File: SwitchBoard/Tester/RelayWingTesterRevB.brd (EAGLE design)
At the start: 77.1 x 67.3 mm, 18 parts

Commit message: Updating tester
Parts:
- added 3VPIN, GNDPIN, SCLPIN, SDAPIN: (no value), adafruit:1X01
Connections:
- removed net N$18: JP2.1, MS1.1
- new net RESET: JP2.1, MS1.1, U$4.14/A0
- net 3V: now also 3VPIN.1
- net GND: now also GNDPIN.1
- net N$2: now also SDAPIN.1
- net SCL: now also SCLPIN.1
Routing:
- net RESET: track 0.00 -> 74.7 mm, vias 0 -> 1
- net 3V: track 101.5 -> 141.5 mm, vias 0 -> 1
- net GND: track 59.1 -> 91.9 mm
- net SCL: track 40.5 -> 54.0 mm
- net N$2: track 46.6 -> 52.8 mm
- net N$56: track 43.1 -> 45.9 mm
- net N$18: track 2.54 -> 0.00 mm
- net N$55: track 47.5 -> 50.0 mm
- net N$57: track 51.7 -> 53.9 mm
- net N$62: track 30.6 -> 29.9 mm

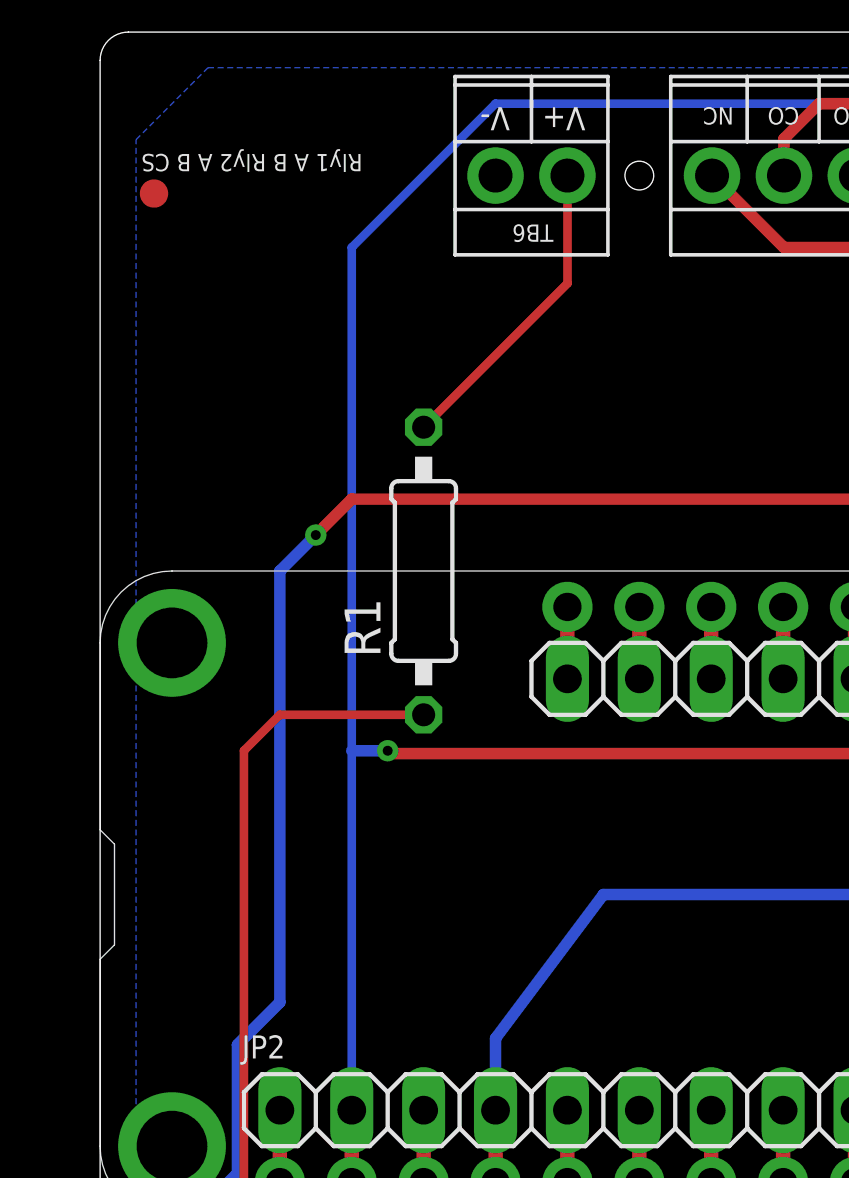
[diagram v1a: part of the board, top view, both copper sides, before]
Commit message: Moved resistor to the ground-side of the current sensor
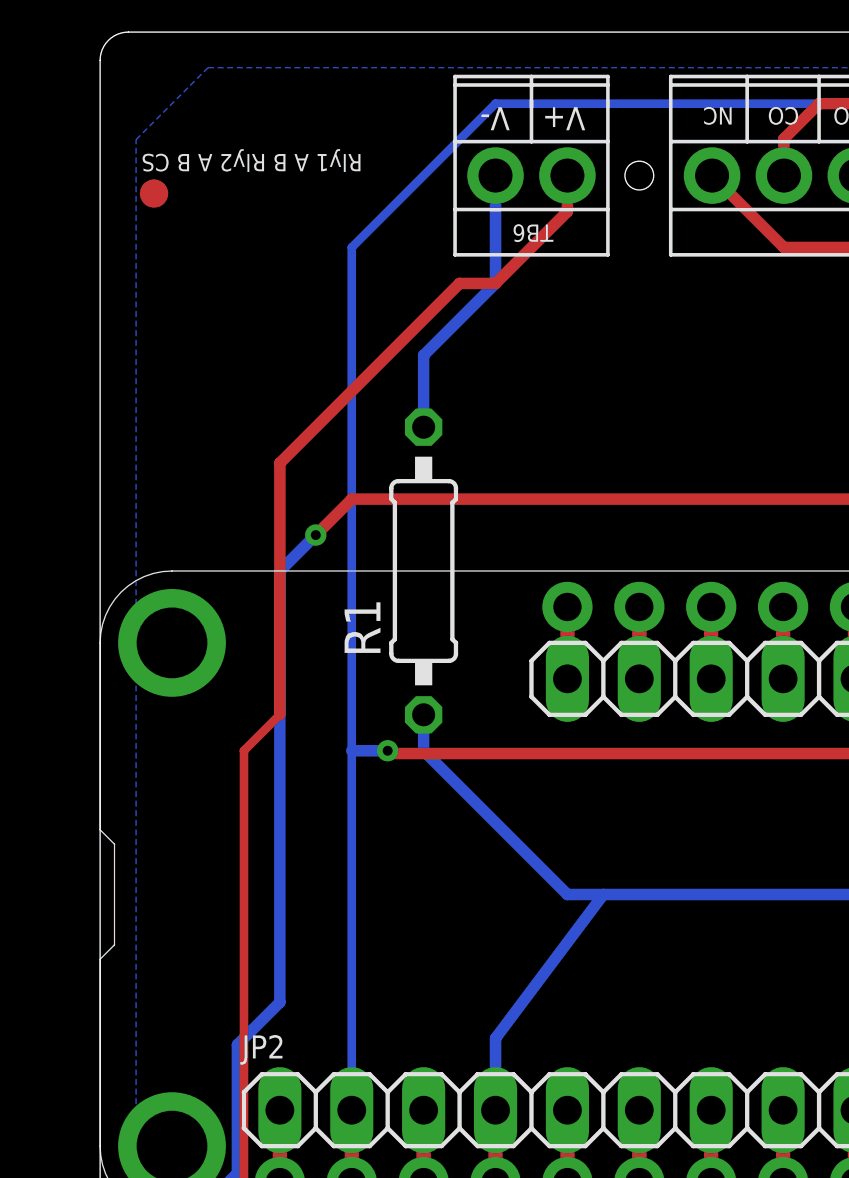
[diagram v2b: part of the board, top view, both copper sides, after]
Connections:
- removed net N$54: R1.2, TB6.1
- new net N$18: R1.2, TB6.2
- net GND: now also R1.1; no longer TB6.2
- net N$53: now also TB6.1; no longer R1.1
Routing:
- net N$53: track 95.6 -> 114.5 mm
- net N$54: track 11.0 -> 0.00 mm
- net N$18: track 0.00 -> 9.94 mm
- net GND: track 91.9 -> 101.7 mm
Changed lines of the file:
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@@
 <drawing>
 <settings>
-<setting alwaysvectorfont="no"/>
+<setting alwaysvectorfont="yes"/>
 <setting verticaltext="up"/>
 </settings>
@@
 <contactref element="JP2" pad="4"/>
 <contactref element="U$4" pad="GND"/>
-<contactref element="TB6" pad="2"/>
 <contactref element="R2" pad="2"/>
 <wire x1="13.97" y1="29.21" x2="13.97" y2="26.67" width="0.508" layer="1"/>
@@
 <wire x1="17.78" y1="36.83" x2="13.97" y2="31.75" width="0.4064" layer="16"/>
 <wire x1="13.97" y1="31.75" x2="13.97" y2="29.21" width="0.4064" layer="16"/>
+<contactref element="R1" pad="1"/>
+<wire x1="11.43" y1="43.18" x2="11.43" y2="41.91" width="0.4064" layer="16"/>
+<wire x1="16.51" y1="36.83" x2="17.78" y2="36.83" width="0.4064" layer="16"/>
+<wire x1="11.43" y1="41.91" x2="16.51" y2="36.83" width="0.4064" layer="16"/>
 </signal>
 <signal name="3V">
@@
 <signal name="N$53">
 <contactref element="U$4" pad="21/DAC0"/>
-<contactref element="R1" pad="1"/>
-<wire x1="11.43" y1="43.18" x2="6.35" y2="43.18" width="0.3048" layer="1"/>
-<wire x1="6.35" y1="43.18" x2="5.08" y2="41.91" width="0.3048" layer="1"/>
+<wire x1="5.08" y1="41.91" x2="6.35" y2="43.18" width="0.3048" layer="1"/>
 <wire x1="5.08" y1="41.91" x2="5.08" y2="22.86" width="0.3048" layer="1"/>
 <wire x1="5.08" y1="22.86" x2="6.35" y2="21.59" width="0.3048" layer="1"/>
 <wire x1="72.39" y1="21.59" x2="73.66" y2="20.32" width="0.3048" layer="1"/>
 <wire x1="6.35" y1="21.59" x2="72.39" y2="21.59" width="0.3048" layer="1"/>
-</signal>
-<signal name="N$54">
-<contactref element="R1" pad="2"/>
 <contactref element="TB6" pad="1"/>
-<wire x1="11.43" y1="53.34" x2="16.51" y2="58.42" width="0.3048" layer="1"/>
-<wire x1="16.51" y1="58.42" x2="16.51" y2="62.23" width="0.3048" layer="1"/>
+<wire x1="6.35" y1="43.18" x2="6.35" y2="52.07" width="0.4064" layer="1"/>
+<wire x1="6.35" y1="52.07" x2="12.7" y2="58.42" width="0.4064" layer="1"/>
+<wire x1="12.7" y1="58.42" x2="13.97" y2="58.42" width="0.4064" layer="1"/>
+<wire x1="13.97" y1="58.42" x2="16.51" y2="60.96" width="0.4064" layer="1"/>
+<wire x1="16.51" y1="60.96" x2="16.51" y2="62.23" width="0.4064" layer="1"/>
 </signal>
 <signal name="N$55">
@@
 <wire x1="4.8514" y1="26.98258125" x2="4.8514" y2="31.5214" width="0.4064" layer="16"/>
 <wire x1="1.27" y1="4.58986875" x2="1.27" y2="23.40118125" width="0.4064" layer="16"/>
-<wire x1="6.35" y1="33.02" x2="6.35" y2="48.26" width="0.4064" layer="16"/>
+<wire x1="6.35" y1="33.02" x2="6.35" y2="43.18" width="0.4064" layer="16"/>
+<wire x1="6.35" y1="43.18" x2="6.35" y2="48.26" width="0.4064" layer="16"/>
 <wire x1="6.35" y1="48.26" x2="7.62" y2="49.53" width="0.4064" layer="16"/>
 <via x="7.62" y="49.53" extent="1-16" drill="0.35"/>
@@
 <wire x1="8.89" y1="22.86" x2="6.35" y2="26.67" width="0.4064" layer="1"/>
 </signal>
+<signal name="N$18">
+<contactref element="TB6" pad="2"/>
+<contactref element="R1" pad="2"/>
+<wire x1="13.97" y1="58.42" x2="11.43" y2="55.88" width="0.4064" layer="16"/>
+<wire x1="11.43" y1="55.88" x2="11.43" y2="53.34" width="0.4064" layer="16"/>
+<wire x1="13.97" y1="62.23" x2="13.97" y2="58.42" width="0.4064" layer="16"/>
+</signal>
 </signals>
